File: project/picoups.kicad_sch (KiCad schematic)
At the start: 22 parts, among them J1 VIN, J2 BATT, J3 USB_C_Receptacle, J4 Conn_02x20_Odd_Even, Q1 Q_PMOS_GSD, SW2 SW_USER, U6 M41T62

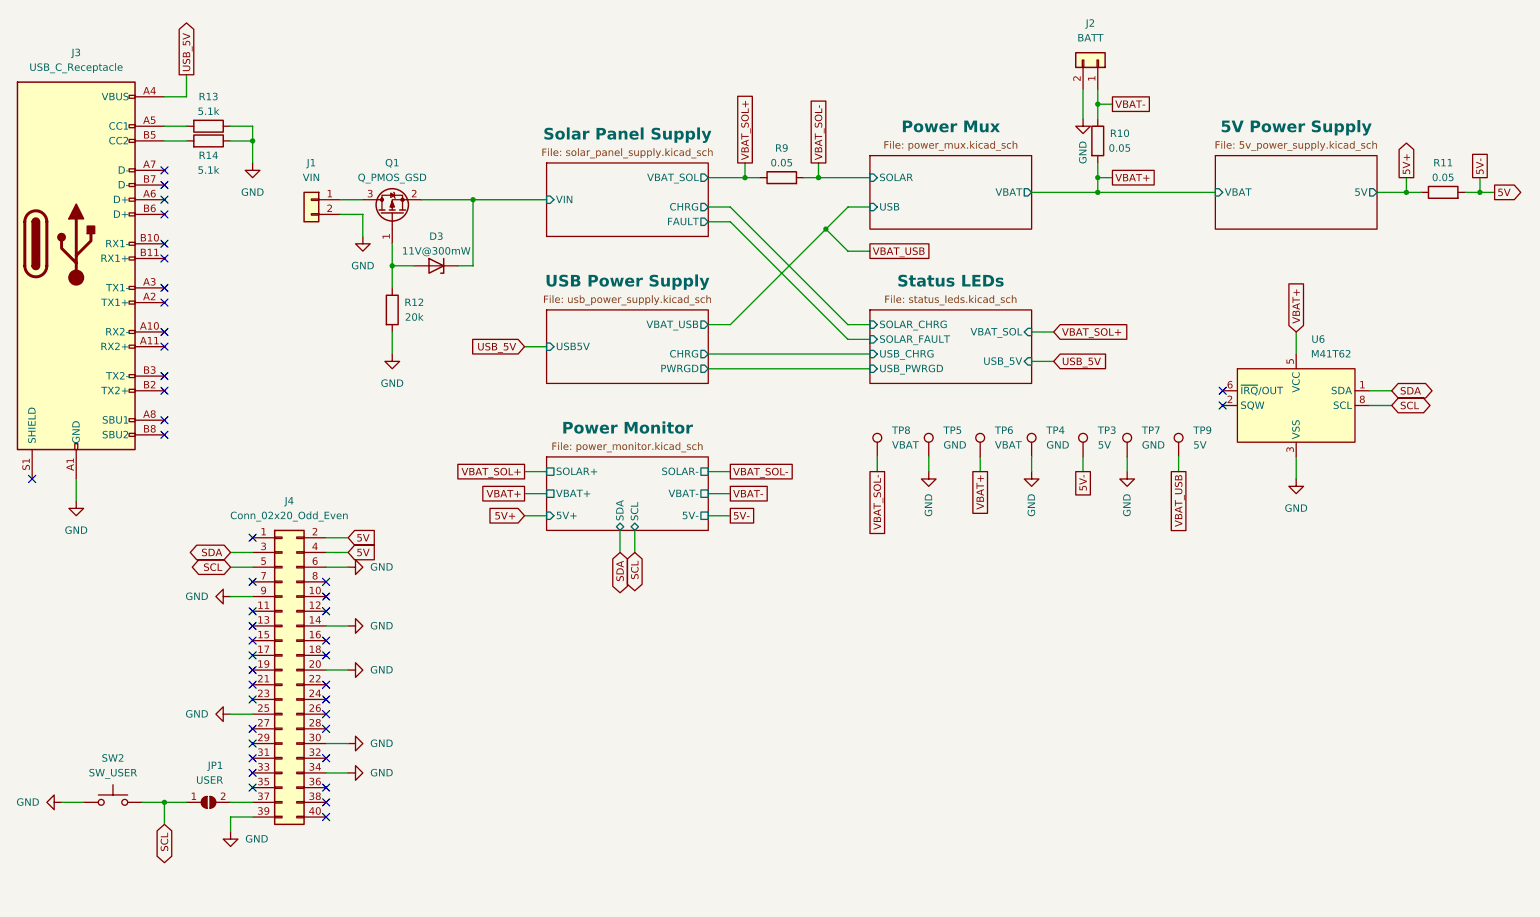
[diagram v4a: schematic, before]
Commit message: Added RTC wake
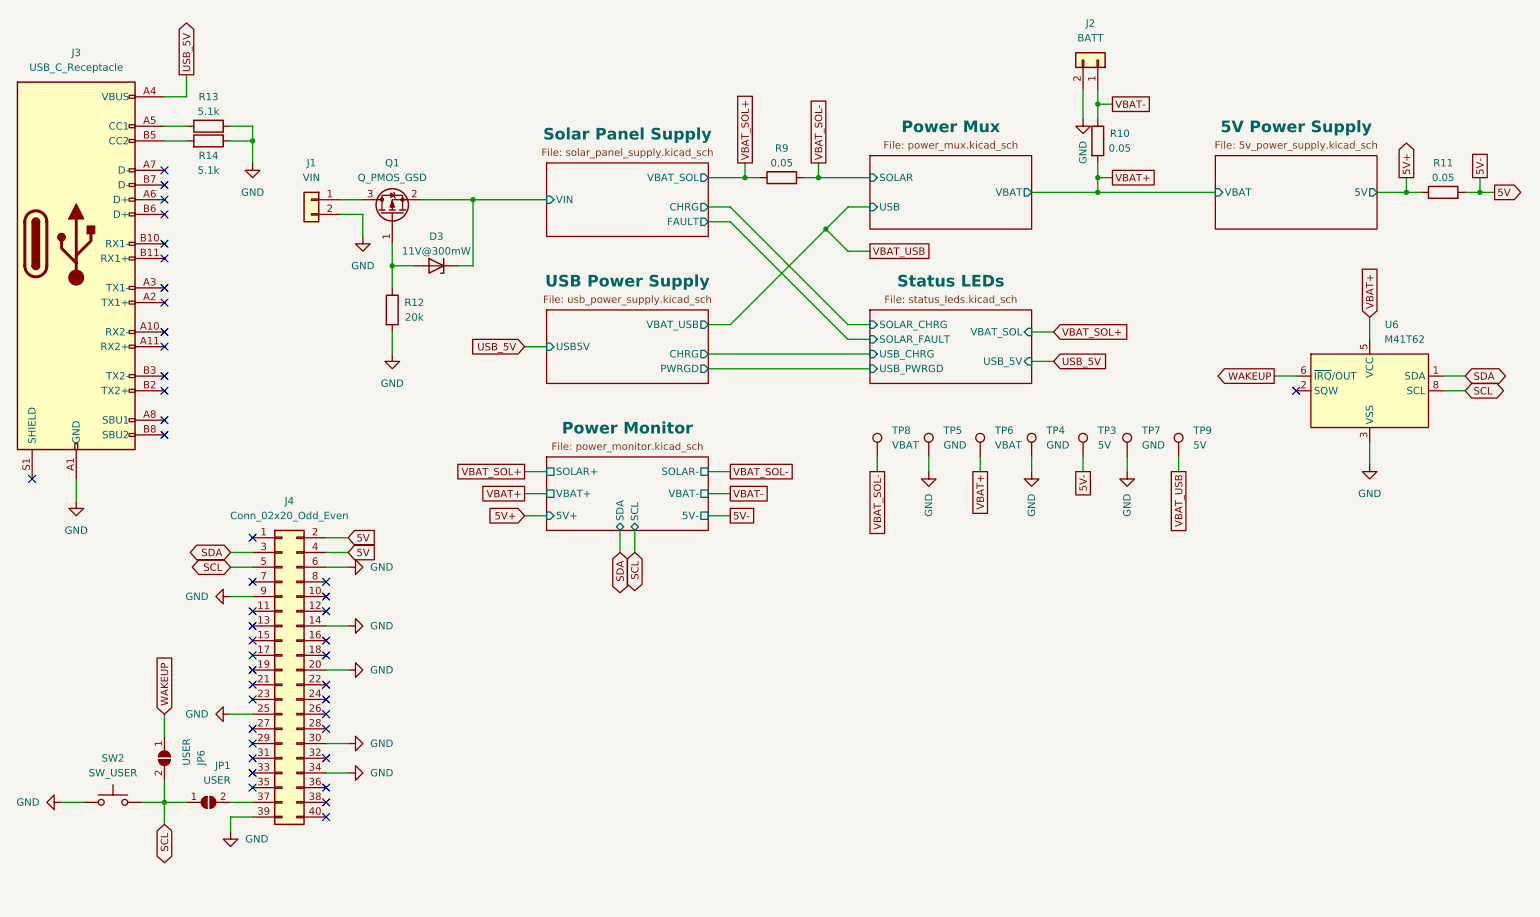
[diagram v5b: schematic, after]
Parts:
- added JP6: USER, Jumper:SolderJumper-2_P1.3mm_Open_RoundedPad1.0x1.5mm, symbol Jumper:SolderJumper_2_Open
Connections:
- net SCL: now also JP6.2 (B)
- net WAKEUP: now reaches U6.6 (~{IRQ}/OUT)
- net WAKEUP: now also JP6.1 (A)
- no-connect marks 44 -> 43
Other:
- moved on the sheet: U6
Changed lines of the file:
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@@
   (no_connect (at 60.96 114.3))
   (no_connect (at 73.66 114.3))
-  (no_connect (at 228.6 83.82))
+  (no_connect (at 241.3 81.28))
   (no_connect (at 73.66 119.38))
-  (no_connect (at 228.6 81.28))
   (no_connect (at 60.96 134.62))
   (no_connect (at 60.96 147.32))
@@
     (stroke (width 0) (type default))
   )
+  (wire (pts (xy 45.72 148.59) (xy 45.72 152.4))
+    (stroke (width 0) (type default))
+  )
   (wire (pts (xy 99.06 59.69) (xy 99.06 48.26))
     (stroke (width 0) (type default))
@@
     (stroke (width 0) (type default))
   )
-  (wire (pts (xy 254 83.82) (xy 257.81 83.82))
+  (wire (pts (xy 266.7 81.28) (xy 270.51 81.28))
     (stroke (width 0) (type default))
   )
@@
     (stroke (width 0) (type default))
   )
-  (wire (pts (xy 254 81.28) (xy 257.81 81.28))
+  (wire (pts (xy 266.7 78.74) (xy 270.51 78.74))
     (stroke (width 0) (type default))
   )
@@
     (stroke (width 0) (type default))
   )
-  (wire (pts (xy 241.3 74.93) (xy 241.3 71.12))
+  (wire (pts (xy 254 72.39) (xy 254 68.58))
     (stroke (width 0) (type default))
   )
@@
     (stroke (width 0) (type default))
   )
+  (wire (pts (xy 45.72 137.16) (xy 45.72 140.97))
+    (stroke (width 0) (type default))
+  )
   (wire (pts (xy 96.52 59.69) (xy 99.06 59.69))
     (stroke (width 0) (type default))
@@
     (stroke (width 0) (type default))
   )
-  (wire (pts (xy 241.3 92.71) (xy 241.3 96.52))
+  (wire (pts (xy 254 90.17) (xy 254 93.98))
     (stroke (width 0) (type default))
   )
@@
     (stroke (width 0) (type default))
   )
+  (wire (pts (xy 237.49 78.74) (xy 241.3 78.74))
+    (stroke (width 0) (type default))
+  )
   (wire (pts (xy 30.48 96.52) (xy 30.48 100.33))
     (stroke (width 0) (type default))
@@
     (stroke (width 0) (type default))
   )
-  (global_label "SDA" (shape bidirectional) (at 257.81 81.28 0) (fields_autoplaced)
-    (effects (font (size 1.27 1.27)) (justify left))
-    (property "Intersheetrefs" "${INTERSHEET_REFS}" (at 265.3952 81.28 0)
+  (global_label "SDA" (shape bidirectional) (at 270.51 78.74 0) (fields_autoplaced)
+    (effects (font (size 1.27 1.27)) (justify left))
+    (property "Intersheetrefs" "${INTERSHEET_REFS}" (at 278.0952 78.74 0)
       (effects (font (size 1.27 1.27)) (justify left) hide)
     )
@@
     )
   )
+  (global_label "WAKEUP" (shape output) (at 237.49 78.74 180) (fields_autoplaced)
+    (effects (font (size 1.27 1.27)) (justify right))
+    (property "Intersheetrefs" "${INTERSHEET_REFS}" (at 226.9453 78.74 0)
+      (effects (font (size 1.27 1.27)) (justify right) hide)
+    )
+  )
   (global_label "USB_5V" (shape input) (at 107.95 73.66 180) (fields_autoplaced)
     (effects (font (size 1.27 1.27)) (justify right))
@@
     )
   )
+  (global_label "WAKEUP" (shape input) (at 45.72 137.16 90) (fields_autoplaced)
+    (effects (font (size 1.27 1.27)) (justify left))
+    (property "Intersheetrefs" "${INTERSHEET_REFS}" (at 45.72 126.6153 90)
+      (effects (font (size 1.27 1.27)) (justify left) hide)
+    )
+  )
   (global_label "VBAT_USB" (shape passive) (at 167.64 57.15 0) (fields_autoplaced)
     (effects (font (size 1.27 1.27)) (justify left))
@@
     )
   )
-  (global_label "SCL" (shape bidirectional) (at 257.81 83.82 0) (fields_autoplaced)
-    (effects (font (size 1.27 1.27)) (justify left))
-    (property "Intersheetrefs" "${INTERSHEET_REFS}" (at 265.3347 83.82 0)
+  (global_label "SCL" (shape bidirectional) (at 270.51 81.28 0) (fields_autoplaced)
+    (effects (font (size 1.27 1.27)) (justify left))
+    (property "Intersheetrefs" "${INTERSHEET_REFS}" (at 278.0347 81.28 0)
       (effects (font (size 1.27 1.27)) (justify left) hide)
     )
@@
     )
   )
-  (global_label "VBAT+" (shape input) (at 241.3 71.12 90) (fields_autoplaced)
-    (effects (font (size 1.27 1.27)) (justify left))
-    (property "Intersheetrefs" "${INTERSHEET_REFS}" (at 241.3 62.1476 90)
+  (global_label "VBAT+" (shape input) (at 254 68.58 90) (fields_autoplaced)
+    (effects (font (size 1.27 1.27)) (justify left))
+    (property "Intersheetrefs" "${INTERSHEET_REFS}" (at 254 59.6076 90)
       (effects (font (size 1.27 1.27)) (justify left) hide)
     )
@@
     )
   )
-  (symbol (lib_id "PicoUPS:M41T62") (at 241.3 83.82 0) (unit 1)
+  (symbol (lib_id "PicoUPS:M41T62") (at 254 81.28 0) (unit 1)
     (in_bom yes) (on_board yes) (dnp no)
-    (property "Reference" "U6" (at 245.11 72.39 0)
-      (effects (font (size 1.27 1.27)))
-    )
-    (property "Value" "M41T62" (at 243.84 74.93 0)
+    (property "Reference" "U6" (at 257.81 69.85 0)
+      (effects (font (size 1.27 1.27)))
+    )
+    (property "Value" "M41T62" (at 256.54 72.39 0)
       (effects (font (size 1.27 1.27)) (justify left))
     )
-    (property "Footprint" "PicoUPS:LCC-8" (at 241.3 83.82 0)
-      (effects (font (size 1.27 1.27)) hide)
-    )
-    (property "Datasheet" "" (at 241.3 83.82 0)
+    (property "Footprint" "PicoUPS:LCC-8" (at 254 81.28 0)
+      (effects (font (size 1.27 1.27)) hide)
+    )
+    (property "Datasheet" "" (at 254 81.28 0)
       (effects (font (size 1.27 1.27)) hide)
     )
@@
   (symbol (lib_id "Jumper:SolderJumper_2_Open") (at 53.34 152.4 0) (mirror x) (unit 1)
     (in_bom yes) (on_board yes) (dnp no)
-    (property "Reference" "JP1" (at 55.88 146.05 0)
+    (property "Reference" "JP1" (at 57.15 146.05 0)
       (effects (font (size 1.27 1.27)) (justify right))
     )
-    (property "Value" "USER" (at 55.88 148.59 0)
+    (property "Value" "USER" (at 57.15 148.59 0)
       (effects (font (size 1.27 1.27)) (justify right))
     )
@@
         (path "/d62f1157-7c2f-4dce-8167-d5624900d267"
           (reference "JP1") (unit 1)
+        )
+        (path "/d62f1157-7c2f-4dce-8167-d5624900d267/e21d3221-edd3-4144-8d1a-91b5737dd9b8"
+          (reference "JP1") (unit 1)
+        )
+      )
+    )
+  )
+  (symbol (lib_id "Jumper:SolderJumper_2_Open") (at 45.72 144.78 90) (mirror x) (unit 1)
+    (in_bom yes) (on_board yes) (dnp no)
+    (property "Reference" "JP6" (at 52.07 146.05 0)
+      (effects (font (size 1.27 1.27)) (justify right))
+    )
+    (property "Value" "USER" (at 49.53 146.05 0)
+      (effects (font (size 1.27 1.27)) (justify right))
+    )
+    (property "Footprint" "Jumper:SolderJumper-2_P1.3mm_Open_RoundedPad1.0x1.5mm" (at 45.72 144.78 0)
+      (effects (font (size 1.27 1.27)) hide)
+    )
+    (property "Datasheet" "~" (at 45.72 144.78 0)
+      (effects (font (size 1.27 1.27)) hide)
+    )
+    (pin "1")
+    (pin "2")
+    (instances
+      (project "picoups"
+        (path "/d62f1157-7c2f-4dce-8167-d5624900d267"
+          (reference "JP6") (unit 1)
         )
         (path "/d62f1157-7c2f-4dce-8167-d5624900d267/e21d3221-edd3-4144-8d1a-91b5737dd9b8"
@@
     )
   )
-  (symbol (lib_id "power:GND") (at 241.3 96.52 0) (unit 1)
-    (in_bom yes) (on_board yes) (dnp no) (fields_autoplaced)
-    (property "Reference" "#PWR032" (at 241.3 102.87 0)
-      (effects (font (size 1.27 1.27)) hide)
-    )
-    (property "Value" "GND" (at 241.3 101.6 0)
-      (effects (font (size 1.27 1.27)))
-    )
-    (property "Footprint" "" (at 241.3 96.52 0)
-      (effects (font (size 1.27 1.27)) hide)
-    )
-    (property "Datasheet" "" (at 241.3 96.52 0)
-      (effects (font (size 1.27 1.27)) hide)
-    )
+  (symbol (lib_id "power:GND") (at 254 93.98 0) (unit 1)
+    (in_bom yes) (on_board yes) (dnp no) (fields_autoplaced)
+    (property "Reference" "#PWR032" (at 254 100.33 0)
+      (effects (font (size 1.27 1.27)) hide)
+    )
+    (property "Value" "GND" (at 254 99.06 0)
+      (effects (font (size 1.27 1.27)))
+    )
+    (property "Footprint" "" (at 254 93.98 0)
+      (effects (font (size 1.27 1.27)) hide)
+    )
+    (property "Datasheet" "" (at 254 93.98 0)
+      (effects (font (size 1.27 1.27)) hide)
+    )

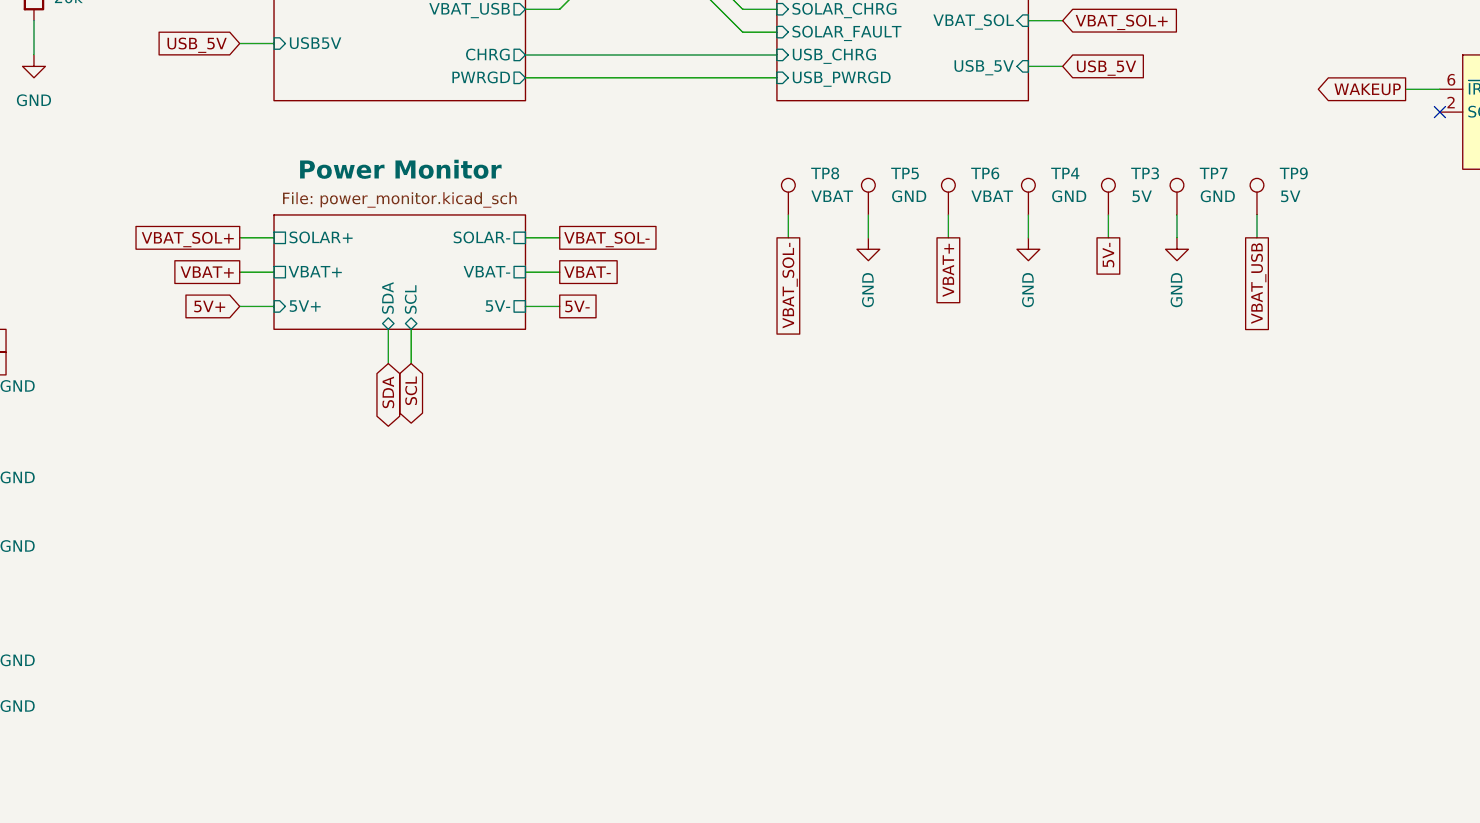
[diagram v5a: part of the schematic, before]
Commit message: Added output capacitors
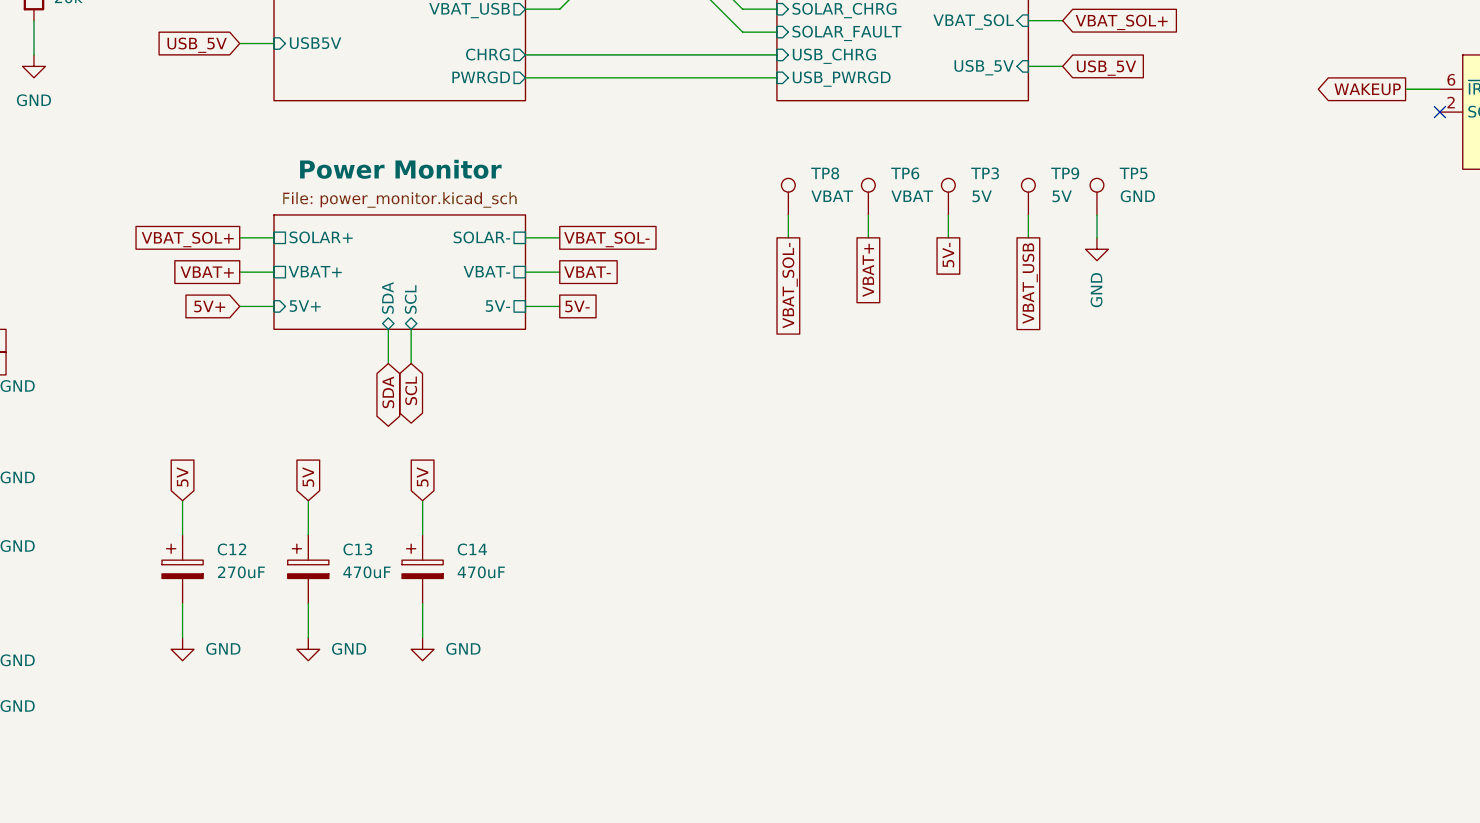
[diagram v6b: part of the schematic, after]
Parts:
- removed TP4, TP7: GND, TestPoint:TestPoint_Pad_D1.0mm, symbol Connector:TestPoint
- added C12: 270uF, Capacitor_SMD:CP_Elec_6.3x5.8, symbol Device:C_Polarized
- added C13, C14: 470uF, Capacitor_SMD:CP_Elec_6.3x7.7, symbol Device:C_Polarized
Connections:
- net 5V: now also C12.1, C13.1, C14.1
- net GND: now also C12.2, C13.2, C14.2
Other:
- moved on the sheet: TP3, TP5, TP6, TP9

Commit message: Final revision
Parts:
- JP6: value USER -> WAKE
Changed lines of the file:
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@@
           (reference "TP3") (unit 1)
-        )
-        (path "/d62f1157-7c2f-4dce-8167-d5624900d267/69257c21-ade6-4c01-a27c-653d8ba74447"
-          (reference "TP2") (unit 1)
         )
       )
@@
         (path "/d62f1157-7c2f-4dce-8167-d5624900d267"
           (reference "R9") (unit 1)
-        )
-        (path "/d62f1157-7c2f-4dce-8167-d5624900d267/28cf3a3e-2270-4421-9985-b09e0cdb49a4"
-          (reference "R7") (unit 1)
         )
       )
@@
           (reference "TP5") (unit 1)
         )
-        (path "/d62f1157-7c2f-4dce-8167-d5624900d267/69257c21-ade6-4c01-a27c-653d8ba74447"
-          (reference "TP2") (unit 1)
-        )
       )
     )
@@
           (reference "R10") (unit 1)
         )
-        (path "/d62f1157-7c2f-4dce-8167-d5624900d267/28cf3a3e-2270-4421-9985-b09e0cdb49a4"
-          (reference "R8") (unit 1)
-        )
       )
     )
@@
           (reference "JP1") (unit 1)
         )
-        (path "/d62f1157-7c2f-4dce-8167-d5624900d267/e21d3221-edd3-4144-8d1a-91b5737dd9b8"
-          (reference "JP1") (unit 1)
-        )
       )
     )
@@
       (effects (font (size 1.27 1.27)) (justify right))
     )
-    (property "Value" "USER" (at 49.53 146.05 0)
+    (property "Value" "WAKE" (at 49.53 146.05 0)
       (effects (font (size 1.27 1.27)) (justify right))
     )
@@
           (reference "JP6") (unit 1)
         )
-        (path "/d62f1157-7c2f-4dce-8167-d5624900d267/e21d3221-edd3-4144-8d1a-91b5737dd9b8"
-          (reference "JP1") (unit 1)
-        )
       )
     )
@@
         (path "/d62f1157-7c2f-4dce-8167-d5624900d267"
           (reference "TP8") (unit 1)
-        )
-        (path "/d62f1157-7c2f-4dce-8167-d5624900d267/69257c21-ade6-4c01-a27c-653d8ba74447"
-          (reference "TP2") (unit 1)
         )
       )
@@
           (reference "TP9") (unit 1)
         )
-        (path "/d62f1157-7c2f-4dce-8167-d5624900d267/69257c21-ade6-4c01-a27c-653d8ba74447"
-          (reference "TP2") (unit 1)
-        )
       )
     )
@@
           (reference "R11") (unit 1)
         )
-        (path "/d62f1157-7c2f-4dce-8167-d5624900d267/28cf3a3e-2270-4421-9985-b09e0cdb49a4"
-          (reference "R9") (unit 1)
-        )
       )
     )
@@
           (reference "SW2") (unit 1)
         )
-        (path "/d62f1157-7c2f-4dce-8167-d5624900d267/92ed0473-53e9-4211-a651-f912f1c2bd2b"
-          (reference "SW1") (unit 1)
-        )
       )
     )
@@
           (reference "TP6") (unit 1)
         )
-        (path "/d62f1157-7c2f-4dce-8167-d5624900d267/69257c21-ade6-4c01-a27c-653d8ba74447"
-          (reference "TP2") (unit 1)
-        )
-      )
+      )
